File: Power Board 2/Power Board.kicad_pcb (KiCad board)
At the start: 4 copper layers, 170 parts, among them IC1 LTC4151IMS#PBF, IC2 LTC4151IMS#PBF, J1 Conn_01x02, J18 Conn_02x03_Top_Bottom, J2 Conn_01x02, J3 Conn_01x02, J4 Conn_01x02, J5 Conn_01x02, J6 Conn_01x02, J7 Conn_01x02, J8 Conn_01x02, J9 Conn_02x03_Top_Bottom, Q1 Q_PMOS_GDS, Q10 Q_NMOS_GDS, Q11 Q_NMOS_GDS, Q12 Q_NMOS_GDS, Q13 Q_NMOS_GDS, Q14 Q_NMOS_GDS, Q15 Q_NMOS_GDS, Q16 Q_NMOS_GDS, Q17 Q_NMOS_GDS, Q18 Q_NMOS_GDS, Q19 Q_NMOS_GDS, Q2 Q_PMOS_GDS, Q20 Q_NMOS_GDS, Q21 Q_NMOS_GDS, Q22 Q_NMOS_GDS, Q3 Q_PMOS_GDS, Q4 Q_PMOS_GDS, Q5 Q_PMOS_GDS, Q6 Q_PMOS_GDS, Q7 Q_PMOS_GDS, Q8 Q_PMOS_GDS, Q9 Q_NMOS_GDS, U1 LTC4372CDD-PBF, U10 ACS770xCB-050U-PFF, U11 ACS770xCB-050U-PFF, U12 ACS770xCB-050U-PFF, U13 ACS770xCB-050U-PFF, U14 ACS770xCB-050U-PFF, U15 ADC128S052CIMT, U17 TLV70033_SOT23-5, U2 LTC4372CDD-PBF, U3 LTC4372CDD-PBF, U4 LTC4372CDD-PBF, U5 LTC4372CDD-PBF, U6 LTC4372CDD-PBF, U7 LTC4372CDD-PBF, U8 ACS770xCB-050U-PFF, U9 ACS770xCB-050U-PFF

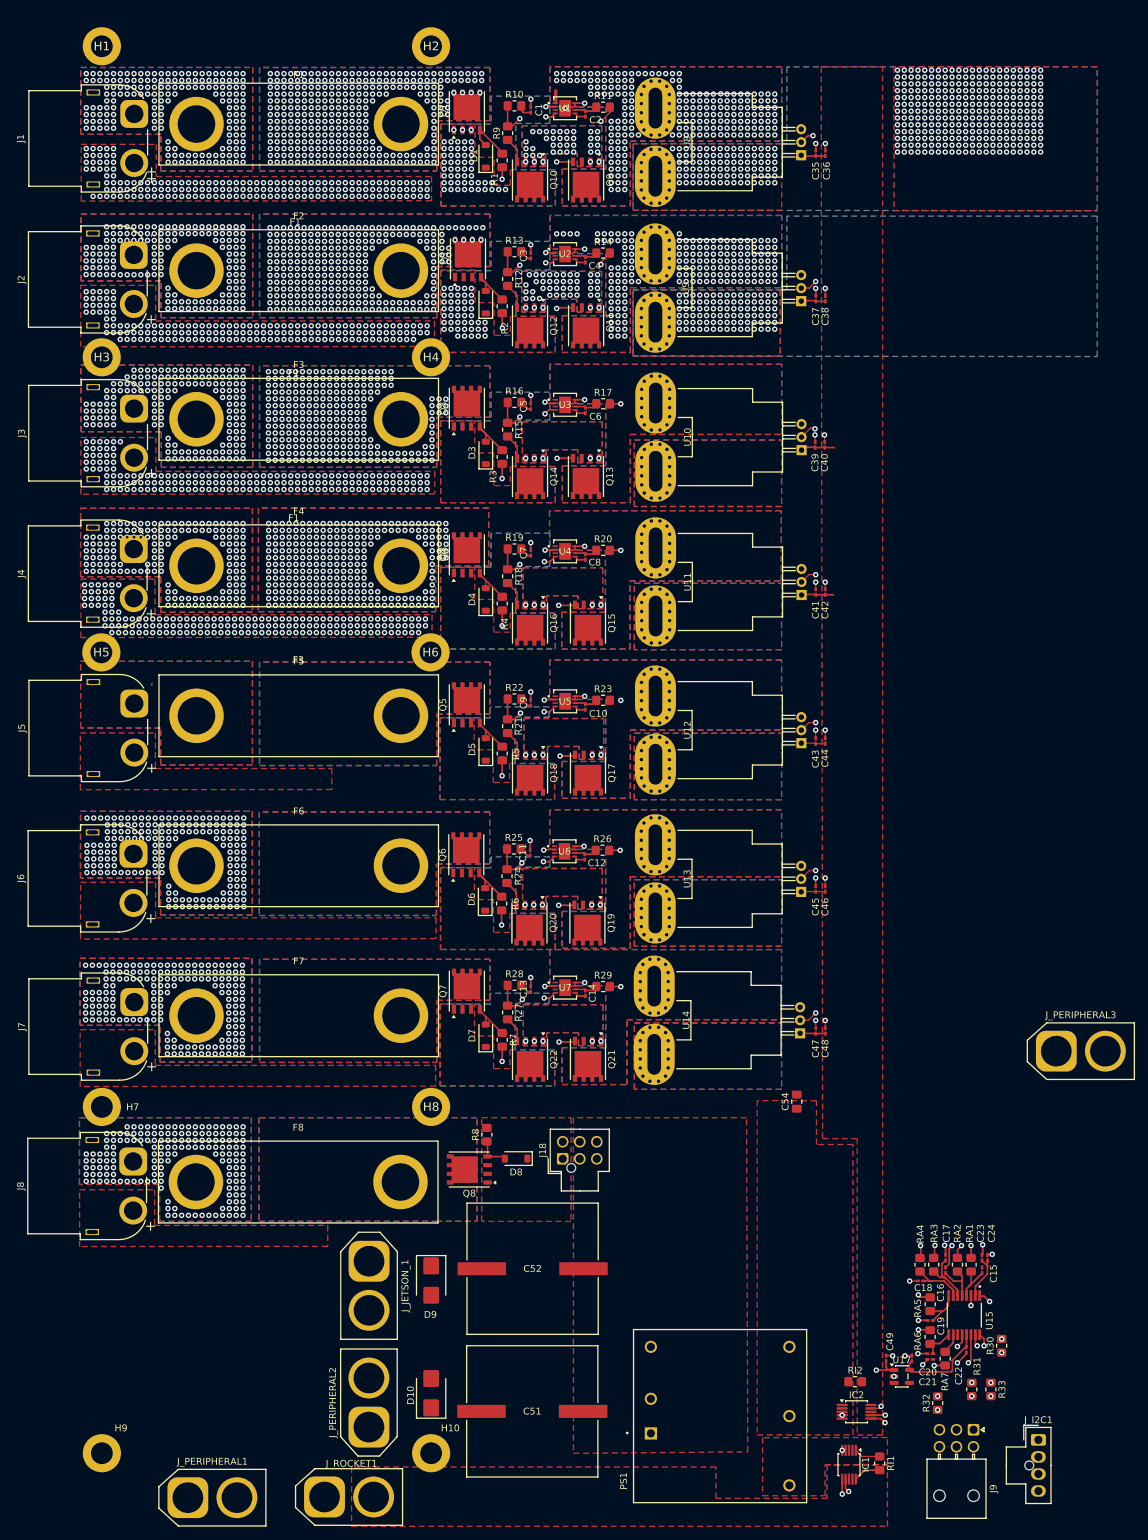
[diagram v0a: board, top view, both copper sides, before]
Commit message: more via stitching
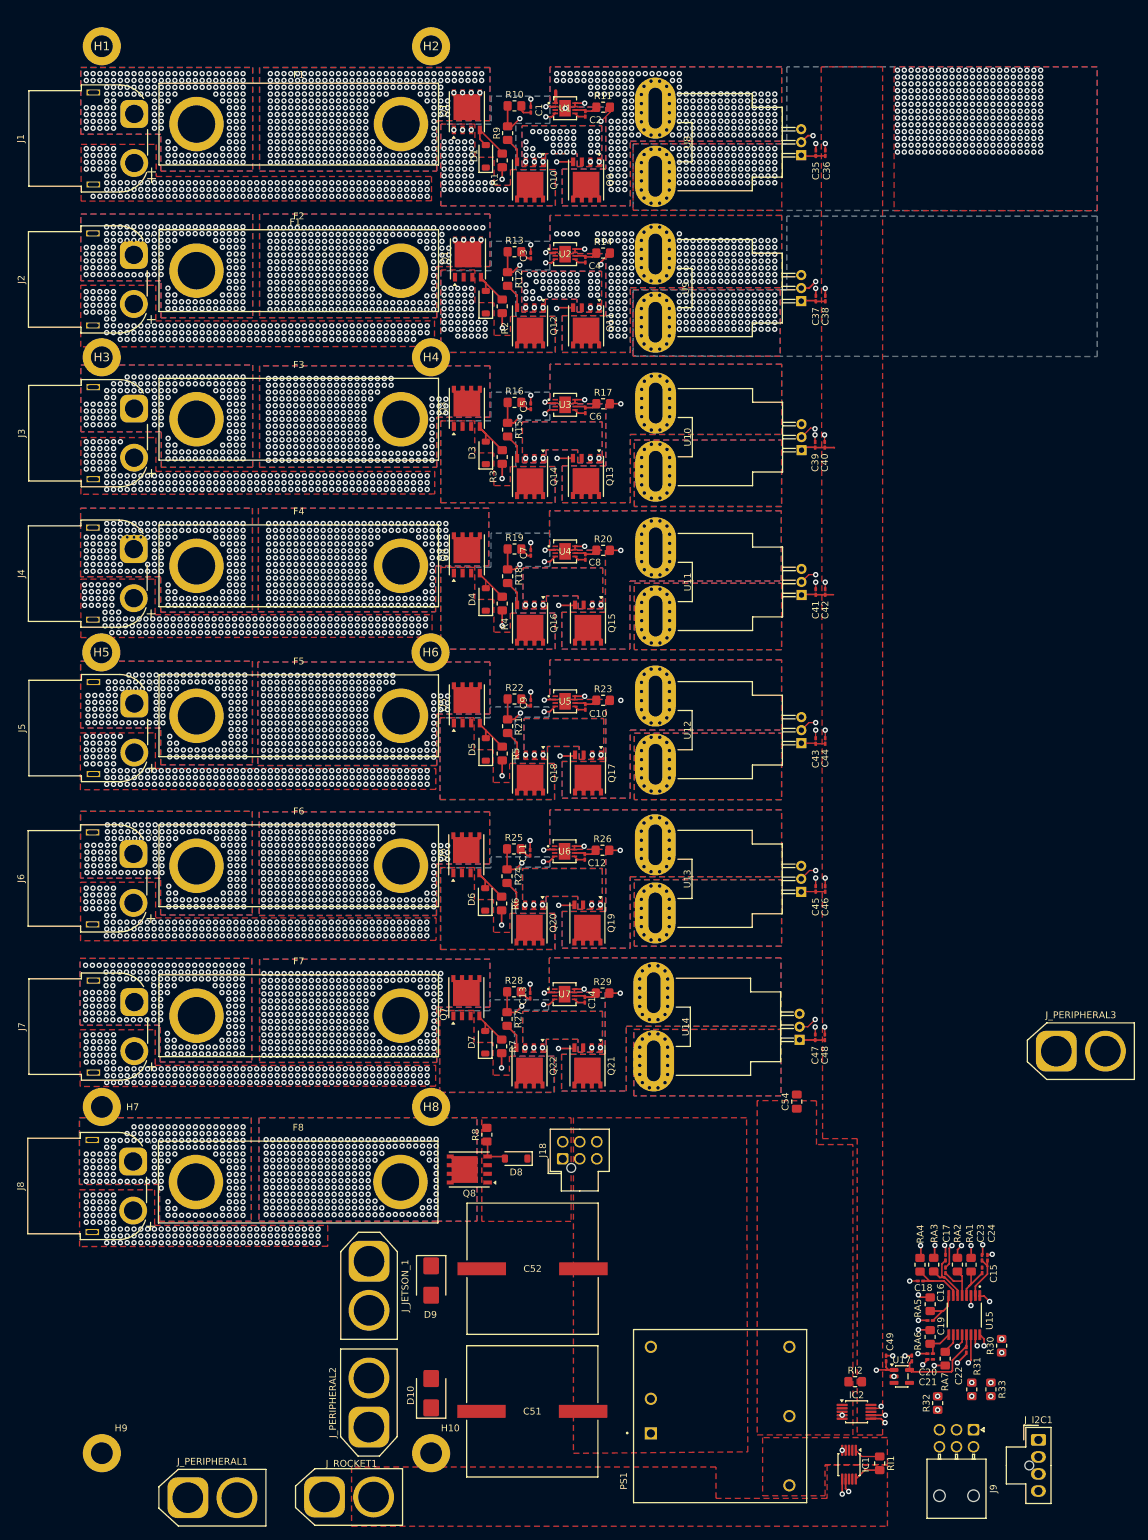
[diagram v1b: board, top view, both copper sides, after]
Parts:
- moved C14 0.96 mm to (123.7, 165.0)
- moved C47 0.96 mm to (157.5, 170.5)
- moved C48 0.96 mm to (158.9, 170.5)
- moved Q7 0.96 mm to (106.3, 164.7)
- moved R27 0.96 mm to (112.3, 167.8)
- moved U14 0.96 mm to (155.2, 170.8)
- moved C13 0.96 mm to (115.7, 164.4)
- moved D7 0.96 mm to (109.1, 171.2)
- moved R28 0.96 mm to (113.3, 163.8)
- moved R29 0.96 mm to (126.3, 164.0)
- moved R7 0.96 mm to (111.5, 171.8)
- moved U7 0.96 mm to (120.7, 164.1)
- moved Q21 0.96 mm to (124.1, 174.7)
- moved Q22 0.96 mm to (115.6, 174.7)
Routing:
- net /BATT_7_SENSE: track 64.4 -> 63.4 mm
- net GND: vias 724 -> 1350
- net Net-(Q8-D): vias 0 -> 243
- net Net-(Q7-D): vias 0 -> 274
- net Net-(Q6-D): vias 0 -> 254
- net Net-(Q5-D): vias 0 -> 260
- net Net-(Q3-D): vias 263 -> 244
- net Net-(J8-Pin_1): vias 166 -> 162
- net Net-(J6-Pin_1): vias 176 -> 152
- net Net-(J5-Pin_1): vias 0 -> 149
- net Net-(J3-Pin_1): vias 157 -> 140
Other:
- board text added: "-"
- board text removed: "F3"
- board text removed: "Q3"

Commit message: pours and vias for battery outputs
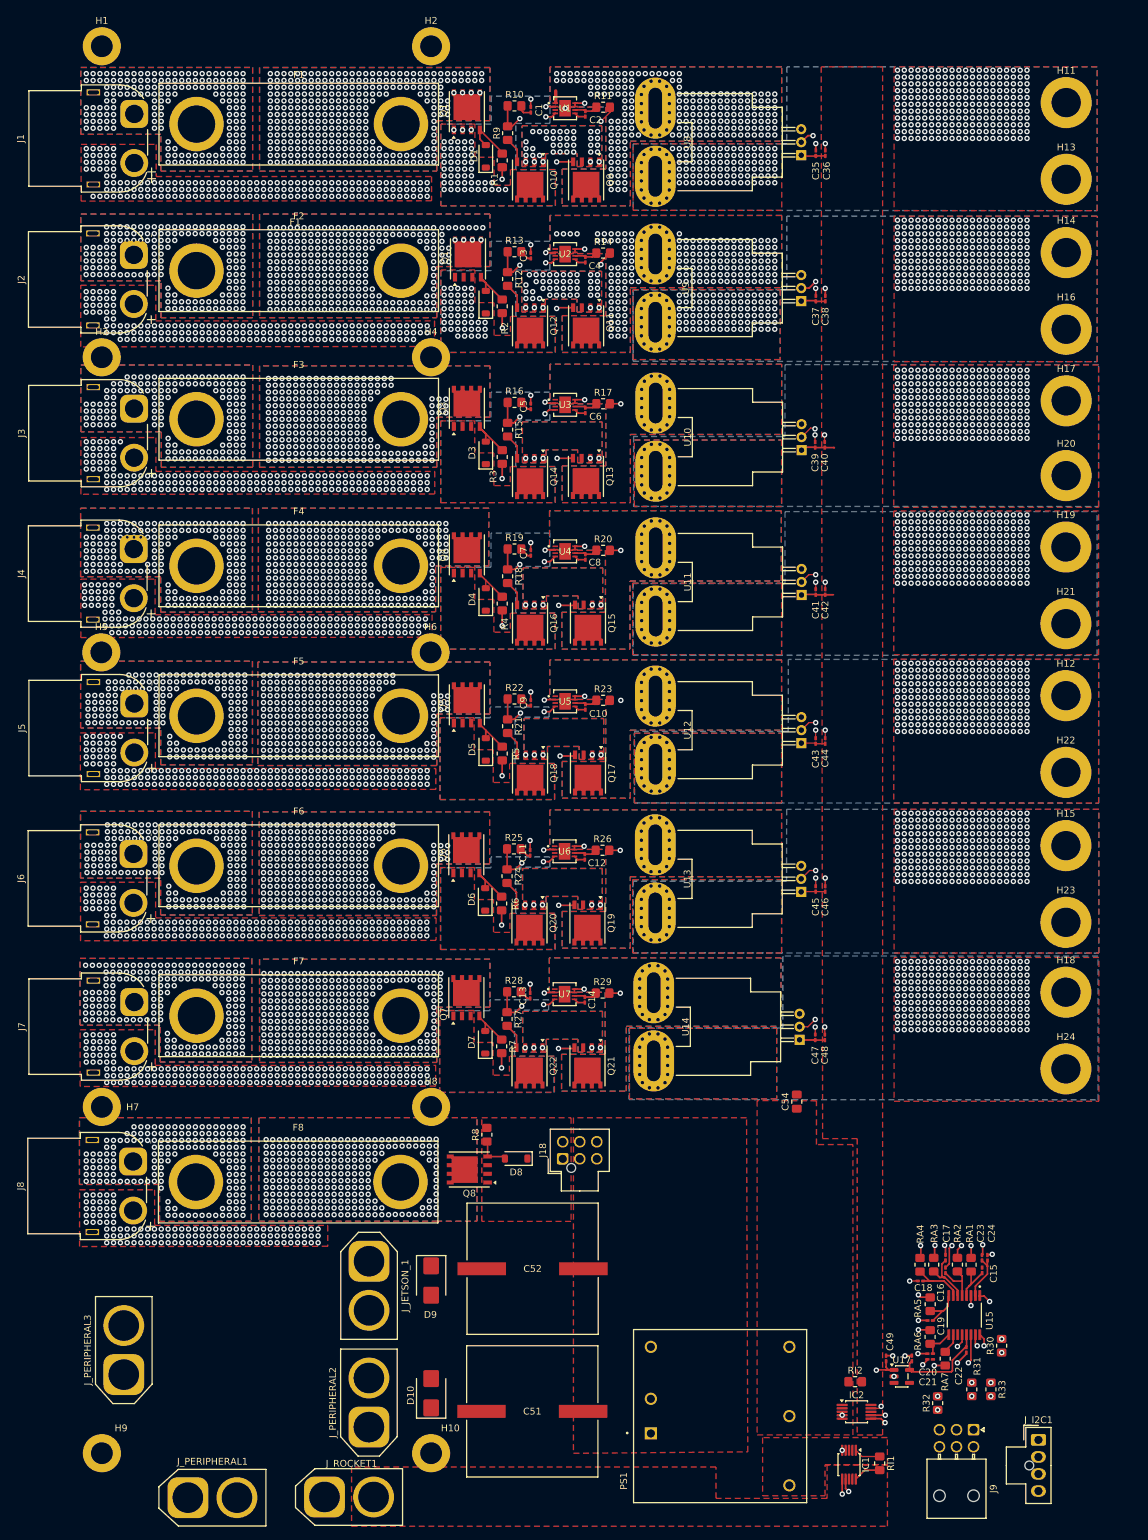
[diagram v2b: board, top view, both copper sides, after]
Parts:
- added H11: MountingHole_Pad, MountingHole:MountingHole_4.3mm_M4_DIN965_Pad, F.Cu at (194.3, 33.4)
- added H12: MountingHole_Pad, MountingHole:MountingHole_4.3mm_M4_DIN965_Pad, F.Cu at (194.3, 120.3)
- added H13: MountingHole_Pad, MountingHole:MountingHole_4.3mm_M4_DIN965_Pad, F.Cu at (194.3, 44.6)
- added H14: MountingHole_Pad, MountingHole:MountingHole_4.3mm_M4_DIN965_Pad, F.Cu at (194.3, 55.4)
- added H15: MountingHole_Pad, MountingHole:MountingHole_4.3mm_M4_DIN965_Pad, F.Cu at (194.3, 142.3)
- added H16: MountingHole_Pad, MountingHole:MountingHole_4.3mm_M4_DIN965_Pad, F.Cu at (194.3, 66.6)
- added H17: MountingHole_Pad, MountingHole:MountingHole_4.3mm_M4_DIN965_Pad, F.Cu at (194.3, 77.1)
- added H18: MountingHole_Pad, MountingHole:MountingHole_4.3mm_M4_DIN965_Pad, F.Cu at (194.3, 163.8)
- added H19: MountingHole_Pad, MountingHole:MountingHole_4.3mm_M4_DIN965_Pad, F.Cu at (194.3, 98.5)
- added H20: MountingHole_Pad, MountingHole:MountingHole_4.3mm_M4_DIN965_Pad, F.Cu at (194.3, 88.1)
- added H21: MountingHole_Pad, MountingHole:MountingHole_4.3mm_M4_DIN965_Pad, F.Cu at (194.3, 109.8)
- added H22: MountingHole_Pad, MountingHole:MountingHole_4.3mm_M4_DIN965_Pad, F.Cu at (194.3, 131.6)
- added H23: MountingHole_Pad, MountingHole:MountingHole_4.3mm_M4_DIN965_Pad, F.Cu at (194.3, 153.6)
- added H24: MountingHole_Pad, MountingHole:MountingHole_4.3mm_M4_DIN965_Pad, F.Cu at (194.3, 175.1)
- H1, H2, H3, H4, H5, H6, H8: footprint (none) -> MountingHole:MountingHole_3.2mm_M3_DIN965_Pad
- moved J_PERIPHERAL3 144.8 mm to (56.1, 219.9), turned to 90 degrees
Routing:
- net /BATT_7_SENSE: track 63.4 -> 63.9 mm
- net /BATT_7: vias 0 -> 220
- net /BATT_6: vias 0 -> 220
- net /BATT_5: vias 0 -> 220
- net /BATT_4: vias 0 -> 220
- net /BATT_3: vias 0 -> 220
- net /BATT_2: vias 90 -> 310
- net /BATT_1: vias 377 -> 311

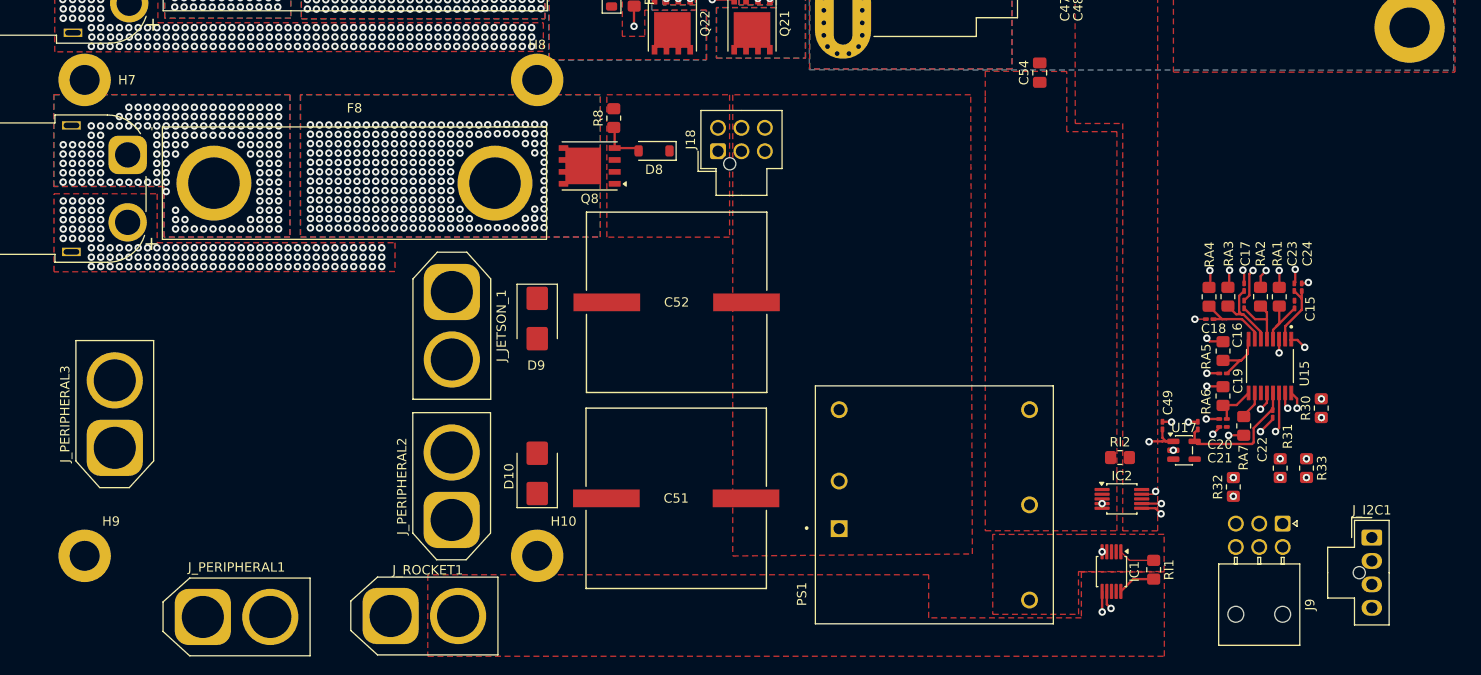
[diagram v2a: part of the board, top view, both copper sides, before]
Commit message: screw terminals for 5V buck, pour + stitching
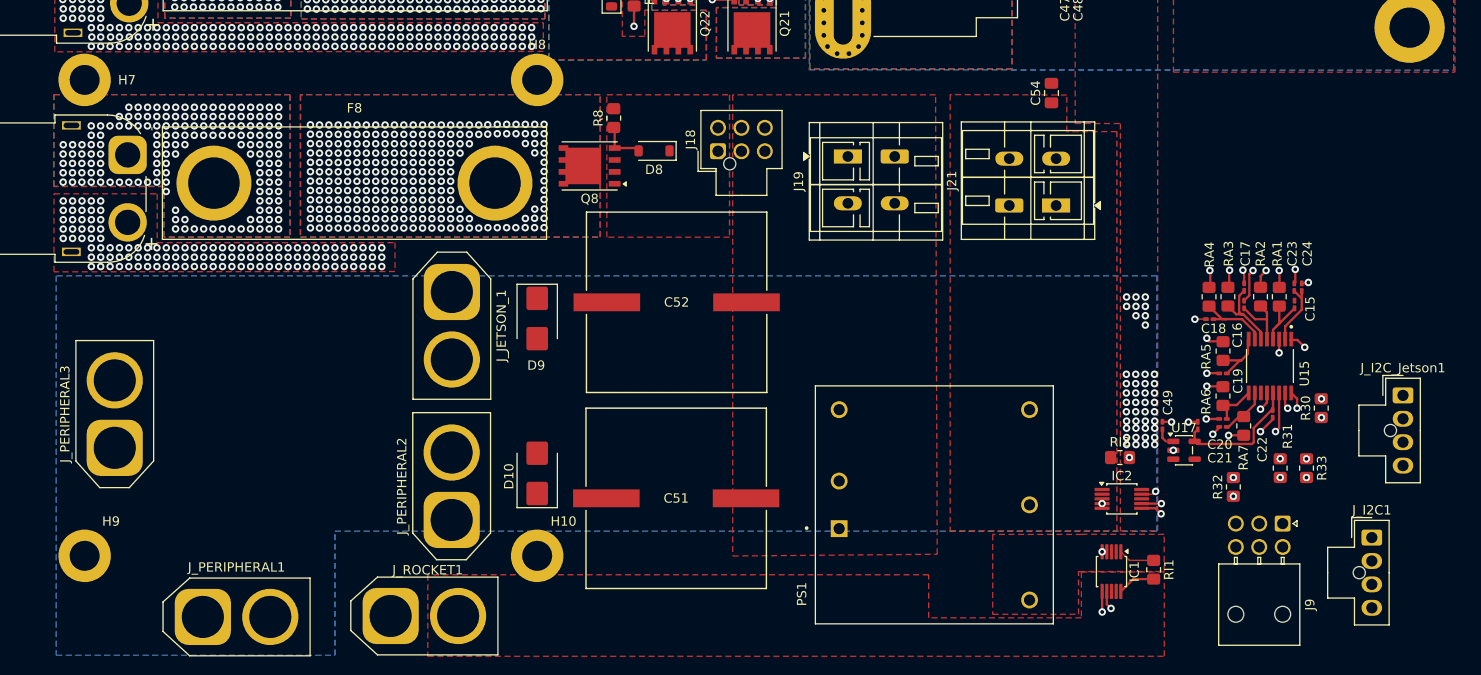
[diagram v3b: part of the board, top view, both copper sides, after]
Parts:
- added J19: Conn_01x02, TerminalBlock_WAGO:TerminalBlock_WAGO_236-402_1x02_P5.00mm_45Degree, F.Cu at (139.3, 188.8)
- added J21: Conn_01x02, TerminalBlock_WAGO:TerminalBlock_WAGO_236-402_1x02_P5.00mm_45Degree, F.Cu at (151.6, 194.1)
- added J_I2C_Jetson1: Conn_02x02_Counter_Clockwise, Connector_Molex:Molex_Nano-Fit_105309-xx04_1x04_P2.50mm_Vertical, F.Cu at (193.6, 214.3)
- moved C54 2.52 mm to (156.1, 182.1)
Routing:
- net /5V_REGULATED: track 39.8 -> 37.2 mm, vias 1 -> 46
- net Net-(U15-IN6): track 3.17 -> 5.35 mm
- added copper zone on B.Cu, net /5V_REGULATED
